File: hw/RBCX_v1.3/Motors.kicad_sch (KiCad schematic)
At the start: 83 parts

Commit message: Work in progress
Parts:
- D10, D11, D12, D13, D5, D6, D7, D8: renamed from D?; footprint Package_TO_SOT_SMD:SOT-23 -> Package_TO_SOT_SMD:SOT-523; LCSC C2828465 -> C134414
- IC3, IC4: renamed from IC?; footprint RBCX:HTSSOP -> RBCX:HTSSOP-16
- U10, U11: renamed from U?; footprint Package_TO_SOT_SMD:SOT-23 -> Package_TO_SOT_SMD:SOT-323_SC-70; LCSC C2762215 -> C57891
- gave numbers to parts that had none: 71
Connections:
- net 3V3: now also D8.1 (A1), U12.3 (VCC), U13.3 (VCC), U6.3 (VCC), U7.3 (VCC); no longer U12.5 (VCC), U13.5 (VCC), U6.5 (VCC), U7.5 (VCC)
- net ENC_1B: now also R89.1
- net GND: now also D8.2 (A2), U12.5 (IN-), U13.5 (IN-), U6.5 (IN-), U7.5 (IN-); no longer U12.4 (IN-), U13.4 (IN-), U6.4 (IN-), U7.4 (IN-)
- net M1GND: now also U6.4 (IN+); no longer U6.3 (IN+)
- net M2GND: now also U7.4 (IN+); no longer U7.3 (IN+)
- net M3GND: now also U12.4 (IN+); no longer U12.3 (IN+)
- net M4GND: now also U13.4 (IN+); no longer U13.3 (IN+)
- net MI1: now also U6.6 (OUT); no longer U6.1 (REF)
- net MI2: now also U7.6 (OUT); no longer U7.1 (REF)
- net MI3: now also U12.6 (OUT); no longer U12.1 (REF)
- net MI4: now also U13.6 (OUT); no longer U13.1 (REF)
- net at D9.2 (A): now also JP8.2 (C)
- net at JP7.2 (C): now also D4.2 (A)

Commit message: Production files
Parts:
- D10, D11, D12, D13, D5, D6, D7, D8, U10, U11, U12, U13, U6, U7: JLCPCB_CORRECTION (none) -> 0;0;180
- J35, J36, TP13, TP14, TP15, TP16, TP17, TP18, TP19, TP20, TP21, TP22, TP23, TP24, TP25, TP26, TP27, TP28, TP29, TP30, TP31, TP32, TP33, TP34, TP35, TP36, TP37: JLCPCB_IGNORE (none) -> 1
- U4, U5, U8, U9: JLCPCB_CORRECTION (none) -> 0;0;180; LCSC C265405 -> C131342

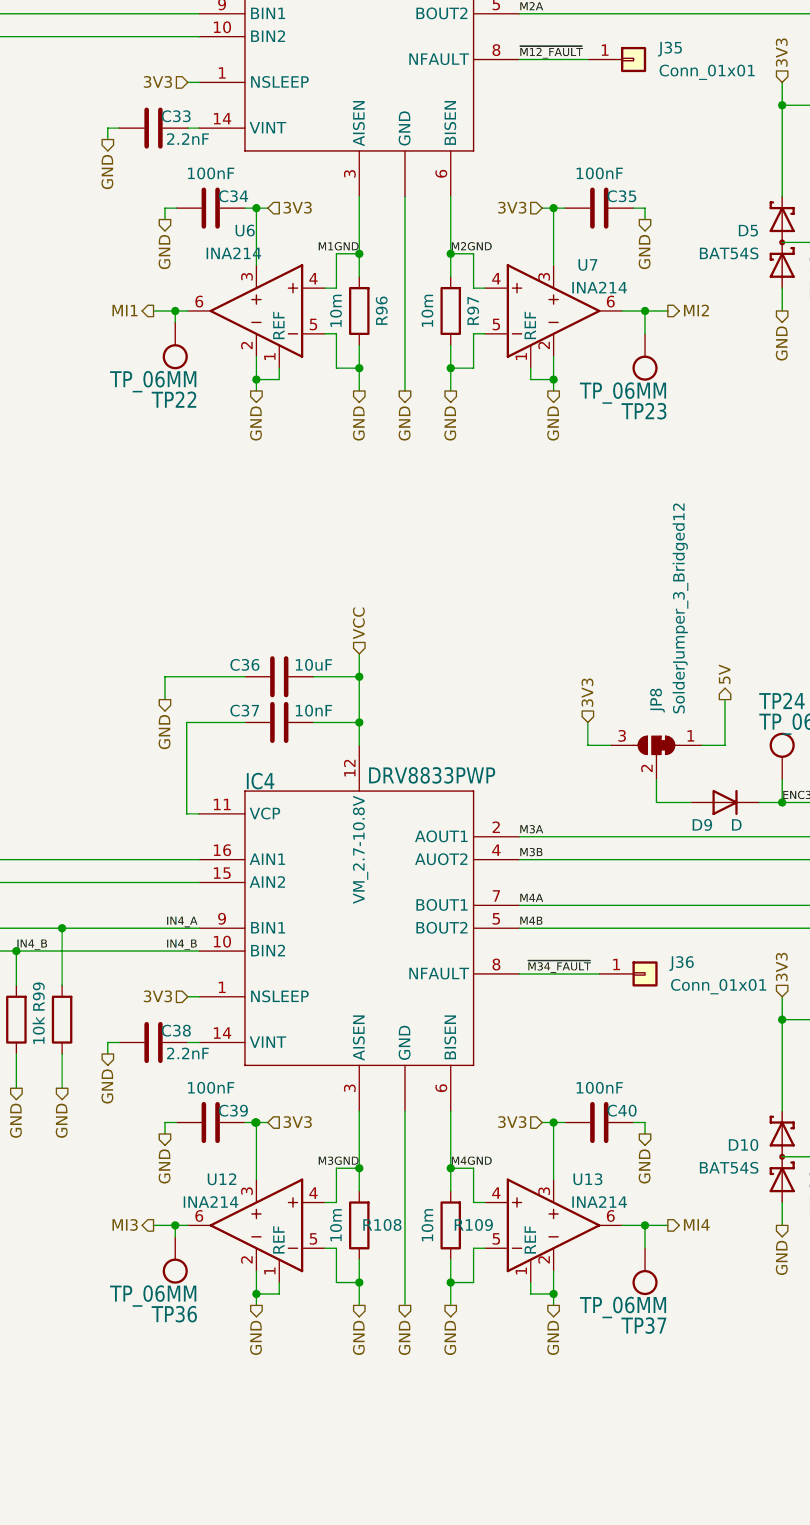
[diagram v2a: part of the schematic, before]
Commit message: Kuba issues
Change of power transistor from JSM3622 to JMSL0302AU

NTC connectors

Moving the Cell balancer behind the switch

and some little things
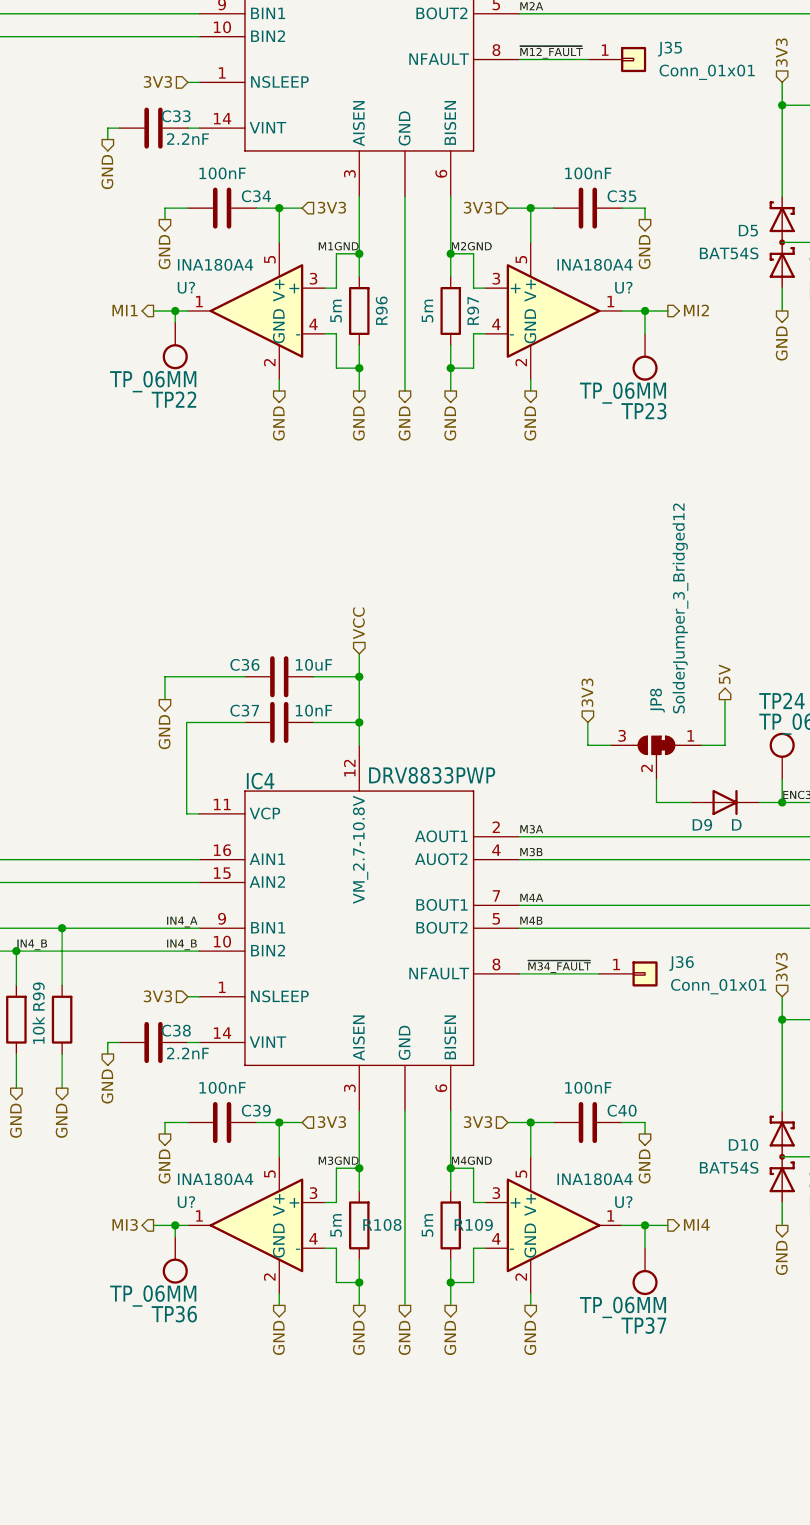
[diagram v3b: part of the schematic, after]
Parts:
- removed U12, U13, U6, U7: INA214, Package_TO_SOT_SMD:SOT-363_SC-70-6, symbol RBCX:INA214
- added U? (x4): INA180A4, Package_TO_SOT_SMD:SOT-23-5, symbol Amplifier_Current:INA180A4
- R108, R109, R96, R97: value 10m -> 5m; LCSC C728271 -> C728267
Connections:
- net 3V3: now also U?.5 (V+), U?.5 (V+), U?.5 (V+), U?.5 (V+)
- net GND: now also U?.2 (GND), U?.2 (GND), U?.2 (GND), U?.2 (GND), U?.4 (-), U?.4 (-), U?.4 (-), U?.4 (-)
- net M1GND: now also U?.3 (+)
- net M2GND: now also U?.3 (+)
- net M3GND: now also U?.3 (+)
- net M4GND: now also U?.3 (+)
- net MI1: now also U?.1
- net MI2: now also U?.1
- net MI3: now also U?.1
- net MI4: now also U?.1
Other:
- moved on the sheet: C34, C35, C39, C40

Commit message: Kuba issues - PCB
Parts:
- gave numbers to parts that had none: 4
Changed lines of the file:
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@@
   (symbol (lib_id "Amplifier_Current:INA180A4") (at 179.07 215.9 0) (mirror y) (unit 1)
     (in_bom yes) (on_board yes)
-    (property "Reference" "U?" (id 0) (at 170.18 213.36 0)
+    (property "Reference" "U12" (id 0) (at 170.18 213.36 0)
       (effects (font (size 1.27 1.27)) (justify right))
     )
@@
   (symbol (lib_id "Amplifier_Current:INA180A4") (at 212.09 114.3 0) (unit 1)
     (in_bom yes) (on_board yes)
-    (property "Reference" "U?" (id 0) (at 220.98 111.76 0)
+    (property "Reference" "U7" (id 0) (at 220.98 111.76 0)
       (effects (font (size 1.27 1.27)) (justify right))
     )
@@
   (symbol (lib_id "Amplifier_Current:INA180A4") (at 212.09 215.9 0) (unit 1)
     (in_bom yes) (on_board yes)
-    (property "Reference" "U?" (id 0) (at 220.98 213.36 0)
+    (property "Reference" "U13" (id 0) (at 220.98 213.36 0)
       (effects (font (size 1.27 1.27)) (justify right))
     )
@@
   (symbol (lib_id "Amplifier_Current:INA180A4") (at 179.07 114.3 0) (mirror y) (unit 1)
     (in_bom yes) (on_board yes)
-    (property "Reference" "U?" (id 0) (at 170.18 111.76 0)
+    (property "Reference" "U6" (id 0) (at 170.18 111.76 0)
       (effects (font (size 1.27 1.27)) (justify right))
     )
